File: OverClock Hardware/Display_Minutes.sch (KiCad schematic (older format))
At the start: 37 parts

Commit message: Completed Schematic and ran ERC
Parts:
- added C28, C29, C30: 10nF, Capacitor_SMD:C_0805_2012Metric_Pad1.15x1.40mm_HandSolder, symbol Device:C_Small
- gave numbers to parts that had none: 37
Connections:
- net GND: now also C28.2, C29.2, C30.2
- net +3V: now reaches U3.43 (Vcc_IO_3)
- net +3V: now also U3.56 (Vcc_IO_3), U3.64 (Vcc_IO_3), C28.1, C29.1, C30.1

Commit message: Matched symbols to footprints and generated netlist
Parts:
- D3, D4: footprint (none) -> Maxted Libs:DSM7TA56106T
- R27, R28, R29, R30, R31, R32, R33, R34, R35, R36, R37, R38, R39, R40, R41, R42: footprint (none) -> Resistor_SMD:R_0805_2012Metric_Pad1.15x1.40mm_HandSolder
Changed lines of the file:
@@
 F 0 "D3" H 13750 3700 50  0000 R CNN
 F 1 "DSM7TA56106T" H 14350 2250 50  0000 R CNN
-F 2 "" H 14450 2900 50  0001 C CNN
+F 2 "Maxted Libs:DSM7TA56106T" H 14450 2900 50  0001 C CNN
 F 3 "" H 14450 2900 50  0001 C CNN
 	1    14150 2900
@@
 F 0 "R27" H 10459 4496 50  0000 L CNN
 F 1 "1K" H 10459 4405 50  0000 L CNN
-F 2 "" H 10400 4450 50  0001 C CNN
+F 2 "Resistor_SMD:R_0805_2012Metric_Pad1.15x1.40mm_HandSolder" H 10400 4450 50  0001 C CNN
 F 3 "~" H 10400 4450 50  0001 C CNN
 	1    10400 4450
@@
 F 0 "R28" H 11009 4496 50  0000 L CNN
 F 1 "1K" H 11009 4405 50  0000 L CNN
-F 2 "" H 10950 4450 50  0001 C CNN
+F 2 "Resistor_SMD:R_0805_2012Metric_Pad1.15x1.40mm_HandSolder" H 10950 4450 50  0001 C CNN
 F 3 "~" H 10950 4450 50  0001 C CNN
 	1    10950 4450
@@
 F 0 "R29" H 11559 4496 50  0000 L CNN
 F 1 "1K" H 11559 4405 50  0000 L CNN
-F 2 "" H 11500 4450 50  0001 C CNN
+F 2 "Resistor_SMD:R_0805_2012Metric_Pad1.15x1.40mm_HandSolder" H 11500 4450 50  0001 C CNN
 F 3 "~" H 11500 4450 50  0001 C CNN
 	1    11500 4450
@@
 F 0 "R30" H 12109 4496 50  0000 L CNN
 F 1 "1K" H 12109 4405 50  0000 L CNN
-F 2 "" H 12050 4450 50  0001 C CNN
+F 2 "Resistor_SMD:R_0805_2012Metric_Pad1.15x1.40mm_HandSolder" H 12050 4450 50  0001 C CNN
 F 3 "~" H 12050 4450 50  0001 C CNN
 	1    12050 4450
@@
 F 0 "R31" H 12659 4496 50  0000 L CNN
 F 1 "1K" H 12659 4405 50  0000 L CNN
-F 2 "" H 12600 4450 50  0001 C CNN
+F 2 "Resistor_SMD:R_0805_2012Metric_Pad1.15x1.40mm_HandSolder" H 12600 4450 50  0001 C CNN
 F 3 "~" H 12600 4450 50  0001 C CNN
 	1    12600 4450
@@
 F 0 "R32" H 13209 4496 50  0000 L CNN
 F 1 "1K" H 13209 4405 50  0000 L CNN
-F 2 "" H 13150 4450 50  0001 C CNN
+F 2 "Resistor_SMD:R_0805_2012Metric_Pad1.15x1.40mm_HandSolder" H 13150 4450 50  0001 C CNN
 F 3 "~" H 13150 4450 50  0001 C CNN
 	1    13150 4450
@@
 F 0 "R33" H 13759 4496 50  0000 L CNN
 F 1 "1K" H 13759 4405 50  0000 L CNN
-F 2 "" H 13700 4450 50  0001 C CNN
+F 2 "Resistor_SMD:R_0805_2012Metric_Pad1.15x1.40mm_HandSolder" H 13700 4450 50  0001 C CNN
 F 3 "~" H 13700 4450 50  0001 C CNN
 	1    13700 4450
@@
 F 0 "R34" H 14359 4496 50  0000 L CNN
 F 1 "1K" H 14359 4405 50  0000 L CNN
-F 2 "" H 14300 4450 50  0001 C CNN
+F 2 "Resistor_SMD:R_0805_2012Metric_Pad1.15x1.40mm_HandSolder" H 14300 4450 50  0001 C CNN
 F 3 "~" H 14300 4450 50  0001 C CNN
 	1    14300 4450
@@
 F 0 "D4" H 7050 3750 50  0000 R CNN
 F 1 "DSM7TA56106T" H 7650 2300 50  0000 R CNN
-F 2 "" H 7750 2950 50  0001 C CNN
+F 2 "Maxted Libs:DSM7TA56106T" H 7750 2950 50  0001 C CNN
 F 3 "" H 7750 2950 50  0001 C CNN
 	1    7450 2950
@@
 F 0 "R35" H 3759 4546 50  0000 L CNN
 F 1 "1K" H 3759 4455 50  0000 L CNN
-F 2 "" H 3700 4500 50  0001 C CNN
+F 2 "Resistor_SMD:R_0805_2012Metric_Pad1.15x1.40mm_HandSolder" H 3700 4500 50  0001 C CNN
 F 3 "~" H 3700 4500 50  0001 C CNN
 	1    3700 4500
@@
 F 0 "R36" H 4309 4546 50  0000 L CNN
 F 1 "1K" H 4309 4455 50  0000 L CNN
-F 2 "" H 4250 4500 50  0001 C CNN
+F 2 "Resistor_SMD:R_0805_2012Metric_Pad1.15x1.40mm_HandSolder" H 4250 4500 50  0001 C CNN
 F 3 "~" H 4250 4500 50  0001 C CNN
 	1    4250 4500
@@
 F 0 "R37" H 4859 4546 50  0000 L CNN
 F 1 "1K" H 4859 4455 50  0000 L CNN
-F 2 "" H 4800 4500 50  0001 C CNN
+F 2 "Resistor_SMD:R_0805_2012Metric_Pad1.15x1.40mm_HandSolder" H 4800 4500 50  0001 C CNN
 F 3 "~" H 4800 4500 50  0001 C CNN
 	1    4800 4500
@@
 F 0 "R38" H 5409 4546 50  0000 L CNN
 F 1 "1K" H 5409 4455 50  0000 L CNN
-F 2 "" H 5350 4500 50  0001 C CNN
+F 2 "Resistor_SMD:R_0805_2012Metric_Pad1.15x1.40mm_HandSolder" H 5350 4500 50  0001 C CNN
 F 3 "~" H 5350 4500 50  0001 C CNN
 	1    5350 4500
@@
 F 0 "R39" H 5959 4546 50  0000 L CNN
 F 1 "1K" H 5959 4455 50  0000 L CNN
-F 2 "" H 5900 4500 50  0001 C CNN
+F 2 "Resistor_SMD:R_0805_2012Metric_Pad1.15x1.40mm_HandSolder" H 5900 4500 50  0001 C CNN
 F 3 "~" H 5900 4500 50  0001 C CNN
 	1    5900 4500
@@
 F 0 "R40" H 6509 4546 50  0000 L CNN
 F 1 "1K" H 6509 4455 50  0000 L CNN
-F 2 "" H 6450 4500 50  0001 C CNN
+F 2 "Resistor_SMD:R_0805_2012Metric_Pad1.15x1.40mm_HandSolder" H 6450 4500 50  0001 C CNN
 F 3 "~" H 6450 4500 50  0001 C CNN
 	1    6450 4500
@@
 F 0 "R41" H 7059 4546 50  0000 L CNN
 F 1 "1K" H 7059 4455 50  0000 L CNN
-F 2 "" H 7000 4500 50  0001 C CNN
+F 2 "Resistor_SMD:R_0805_2012Metric_Pad1.15x1.40mm_HandSolder" H 7000 4500 50  0001 C CNN
 F 3 "~" H 7000 4500 50  0001 C CNN
 	1    7000 4500
@@
 F 0 "R42" H 7659 4546 50  0000 L CNN
 F 1 "1K" H 7659 4455 50  0000 L CNN
-F 2 "" H 7600 4500 50  0001 C CNN
+F 2 "Resistor_SMD:R_0805_2012Metric_Pad1.15x1.40mm_HandSolder" H 7600 4500 50  0001 C CNN
 F 3 "~" H 7600 4500 50  0001 C CNN
 	1    7600 4500

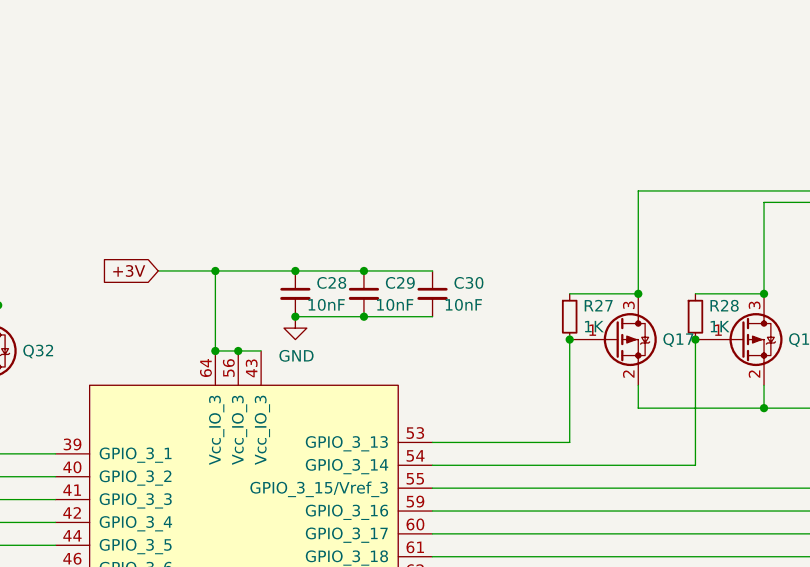
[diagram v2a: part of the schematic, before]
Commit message: Place and route Decoupling Capacitors
Placed and routed all the decoupling capacitors for the FPGA. Created Top and bottom GND planes too for better signal integrity
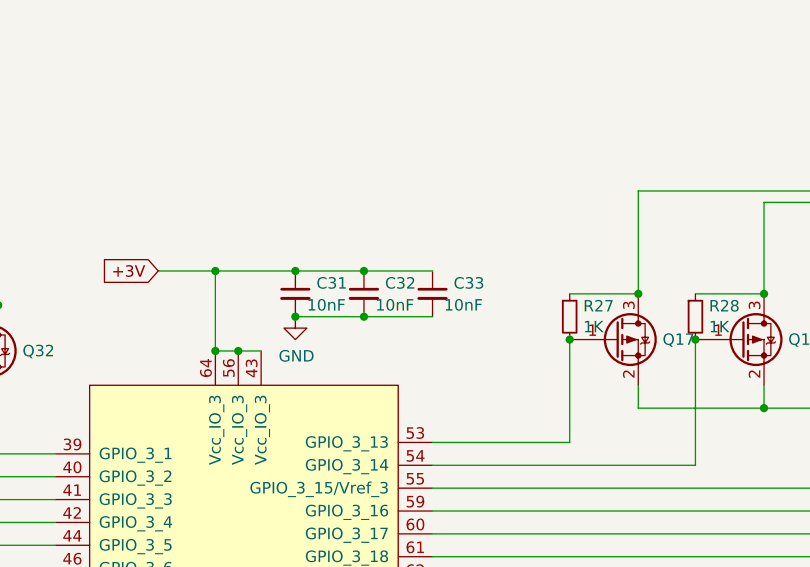
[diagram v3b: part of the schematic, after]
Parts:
- C31: renamed from C28; footprint Capacitor_SMD:C_0805_2012Metric_Pad1.15x1.40mm_HandSolder -> Capacitor_SMD:C_0603_1608Metric_Pad1.05x0.95mm_HandSolder
- C32: renamed from C29; footprint Capacitor_SMD:C_0805_2012Metric_Pad1.15x1.40mm_HandSolder -> Capacitor_SMD:C_0603_1608Metric_Pad1.05x0.95mm_HandSolder
- C33: renamed from C30; footprint Capacitor_SMD:C_0805_2012Metric_Pad1.15x1.40mm_HandSolder -> Capacitor_SMD:C_0603_1608Metric_Pad1.05x0.95mm_HandSolder
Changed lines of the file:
@@
 AR Path="/5C66B7E8/5C9F0D8B" Ref="#PWR?"  Part="1"
 AR Path="/5C87E0ED/5C9F0D8B" Ref="#PWR?"  Part="1"
-AR Path="/5C9EFB73/5C9F0D8B" Ref="#PWR018"  Part="1"
-F 0 "#PWR018" H 14250 1750 50  0001 C CNN
+AR Path="/5C9EFB73/5C9F0D8B" Ref="#PWR019"  Part="1"
+F 0 "#PWR019" H 14250 1750 50  0001 C CNN
 F 1 "+4V" H 14265 2073 50  0000 C CNN
 F 2 "" H 14250 1900 50  0001 C CNN
@@
 AR Path="/5C66B7E8/5C9F0DB7" Ref="#PWR?"  Part="1"
 AR Path="/5C87E0ED/5C9F0DB7" Ref="#PWR?"  Part="1"
-AR Path="/5C9EFB73/5C9F0DB7" Ref="#PWR021"  Part="1"
-F 0 "#PWR021" H 12500 4600 50  0001 C CNN
+AR Path="/5C9EFB73/5C9F0DB7" Ref="#PWR022"  Part="1"
+F 0 "#PWR022" H 12500 4600 50  0001 C CNN
 F 1 "GND" H 12505 4677 50  0000 C CNN
 F 2 "" H 12500 4850 50  0001 C CNN
@@
 AR Path="/5C66B7E8/5C9F3321" Ref="#PWR?"  Part="1"
 AR Path="/5C87E0ED/5C9F3321" Ref="#PWR?"  Part="1"
-AR Path="/5C9EFB73/5C9F3321" Ref="#PWR019"  Part="1"
-F 0 "#PWR019" H 7550 1800 50  0001 C CNN
+AR Path="/5C9EFB73/5C9F3321" Ref="#PWR020"  Part="1"
+F 0 "#PWR020" H 7550 1800 50  0001 C CNN
 F 1 "+4V" H 7565 2123 50  0000 C CNN
 F 2 "" H 7550 1950 50  0001 C CNN
@@
 AR Path="/5C66B7E8/5C9F334D" Ref="#PWR?"  Part="1"
 AR Path="/5C87E0ED/5C9F334D" Ref="#PWR?"  Part="1"
-AR Path="/5C9EFB73/5C9F334D" Ref="#PWR022"  Part="1"
-F 0 "#PWR022" H 5800 4650 50  0001 C CNN
+AR Path="/5C9EFB73/5C9F334D" Ref="#PWR023"  Part="1"
+F 0 "#PWR023" H 5800 4650 50  0001 C CNN
 F 1 "GND" H 5805 4727 50  0000 C CNN
 F 2 "" H 5800 4900 50  0001 C CNN
@@
 	8950 4600 8850 4600
 $Comp
-L Device:C_Small C29
+L Device:C_Small C32
 U 1 1 5CB8F75B
 P 9500 4350
-F 0 "C29" H 9592 4396 50  0000 L CNN
+F 0 "C32" H 9592 4396 50  0000 L CNN
 F 1 "10nF" H 9550 4300 50  0000 L CNN
-F 2 "Capacitor_SMD:C_0805_2012Metric_Pad1.15x1.40mm_HandSolder" H 9500 4350 50  0001 C CNN
+F 2 "Capacitor_SMD:C_0603_1608Metric_Pad1.05x0.95mm_HandSolder" H 9500 4350 50  0001 C CNN
 F 3 "~" H 9500 4350 50  0001 C CNN
 	1    9500 4350
@@
 $EndComp
 $Comp
-L Device:C_Small C30
+L Device:C_Small C33
 U 1 1 5CB8F8E1
 P 9800 4350
-F 0 "C30" H 9892 4396 50  0000 L CNN
+F 0 "C33" H 9892 4396 50  0000 L CNN
 F 1 "10nF" H 9850 4300 50  0000 L CNN
-F 2 "Capacitor_SMD:C_0805_2012Metric_Pad1.15x1.40mm_HandSolder" H 9800 4350 50  0001 C CNN
+F 2 "Capacitor_SMD:C_0603_1608Metric_Pad1.05x0.95mm_HandSolder" H 9800 4350 50  0001 C CNN
 F 3 "~" H 9800 4350 50  0001 C CNN
 	1    9800 4350
@@
 $EndComp
 $Comp
-L Device:C_Small C28
+L Device:C_Small C31
 U 1 1 5CB98270
 P 9200 4350
-F 0 "C28" H 9292 4396 50  0000 L CNN
+F 0 "C31" H 9292 4396 50  0000 L CNN
 F 1 "10nF" H 9250 4300 50  0000 L CNN
-F 2 "Capacitor_SMD:C_0805_2012Metric_Pad1.15x1.40mm_HandSolder" H 9200 4350 50  0001 C CNN
+F 2 "Capacitor_SMD:C_0603_1608Metric_Pad1.05x0.95mm_HandSolder" H 9200 4350 50  0001 C CNN
 F 3 "~" H 9200 4350 50  0001 C CNN
 	1    9200 4350
@@
 	9500 4450 9200 4450
 $Comp
-L power:GND #PWR020
+L power:GND #PWR021
 U 1 1 5CBB2B7C
 P 9200 4450
-F 0 "#PWR020" H 9200 4200 50  0001 C CNN
+F 0 "#PWR021" H 9200 4200 50  0001 C CNN
 F 1 "GND" H 9205 4277 50  0000 C CNN
 F 2 "" H 9200 4450 50  0001 C CNN

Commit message: Completed Initial Routing
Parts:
- R27, R28, R29, R30, R31, R32, R33, R34, R35, R36, R37, R38, R39, R40, R41, R42: footprint Resistor_SMD:R_0805_2012Metric_Pad1.15x1.40mm_HandSolder -> Resistor_SMD:R_0603_1608Metric_Pad1.05x0.95mm_HandSolder
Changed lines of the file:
@@
 F 0 "R27" H 10459 4496 50  0000 L CNN
 F 1 "1K" H 10459 4405 50  0000 L CNN
-F 2 "Resistor_SMD:R_0805_2012Metric_Pad1.15x1.40mm_HandSolder" H 10400 4450 50  0001 C CNN
+F 2 "Resistor_SMD:R_0603_1608Metric_Pad1.05x0.95mm_HandSolder" H 10400 4450 50  0001 C CNN
 F 3 "~" H 10400 4450 50  0001 C CNN
 	1    10400 4450
@@
 F 0 "R28" H 11009 4496 50  0000 L CNN
 F 1 "1K" H 11009 4405 50  0000 L CNN
-F 2 "Resistor_SMD:R_0805_2012Metric_Pad1.15x1.40mm_HandSolder" H 10950 4450 50  0001 C CNN
+F 2 "Resistor_SMD:R_0603_1608Metric_Pad1.05x0.95mm_HandSolder" H 10950 4450 50  0001 C CNN
 F 3 "~" H 10950 4450 50  0001 C CNN
 	1    10950 4450
@@
 F 0 "R29" H 11559 4496 50  0000 L CNN
 F 1 "1K" H 11559 4405 50  0000 L CNN
-F 2 "Resistor_SMD:R_0805_2012Metric_Pad1.15x1.40mm_HandSolder" H 11500 4450 50  0001 C CNN
+F 2 "Resistor_SMD:R_0603_1608Metric_Pad1.05x0.95mm_HandSolder" H 11500 4450 50  0001 C CNN
 F 3 "~" H 11500 4450 50  0001 C CNN
 	1    11500 4450
@@
 F 0 "R30" H 12109 4496 50  0000 L CNN
 F 1 "1K" H 12109 4405 50  0000 L CNN
-F 2 "Resistor_SMD:R_0805_2012Metric_Pad1.15x1.40mm_HandSolder" H 12050 4450 50  0001 C CNN
+F 2 "Resistor_SMD:R_0603_1608Metric_Pad1.05x0.95mm_HandSolder" H 12050 4450 50  0001 C CNN
 F 3 "~" H 12050 4450 50  0001 C CNN
 	1    12050 4450
@@
 F 0 "R31" H 12659 4496 50  0000 L CNN
 F 1 "1K" H 12659 4405 50  0000 L CNN
-F 2 "Resistor_SMD:R_0805_2012Metric_Pad1.15x1.40mm_HandSolder" H 12600 4450 50  0001 C CNN
+F 2 "Resistor_SMD:R_0603_1608Metric_Pad1.05x0.95mm_HandSolder" H 12600 4450 50  0001 C CNN
 F 3 "~" H 12600 4450 50  0001 C CNN
 	1    12600 4450
@@
 F 0 "R32" H 13209 4496 50  0000 L CNN
 F 1 "1K" H 13209 4405 50  0000 L CNN
-F 2 "Resistor_SMD:R_0805_2012Metric_Pad1.15x1.40mm_HandSolder" H 13150 4450 50  0001 C CNN
+F 2 "Resistor_SMD:R_0603_1608Metric_Pad1.05x0.95mm_HandSolder" H 13150 4450 50  0001 C CNN
 F 3 "~" H 13150 4450 50  0001 C CNN
 	1    13150 4450
@@
 F 0 "R33" H 13759 4496 50  0000 L CNN
 F 1 "1K" H 13759 4405 50  0000 L CNN
-F 2 "Resistor_SMD:R_0805_2012Metric_Pad1.15x1.40mm_HandSolder" H 13700 4450 50  0001 C CNN
+F 2 "Resistor_SMD:R_0603_1608Metric_Pad1.05x0.95mm_HandSolder" H 13700 4450 50  0001 C CNN
 F 3 "~" H 13700 4450 50  0001 C CNN
 	1    13700 4450
@@
 F 0 "R34" H 14359 4496 50  0000 L CNN
 F 1 "1K" H 14359 4405 50  0000 L CNN
-F 2 "Resistor_SMD:R_0805_2012Metric_Pad1.15x1.40mm_HandSolder" H 14300 4450 50  0001 C CNN
+F 2 "Resistor_SMD:R_0603_1608Metric_Pad1.05x0.95mm_HandSolder" H 14300 4450 50  0001 C CNN
 F 3 "~" H 14300 4450 50  0001 C CNN
 	1    14300 4450
@@
 F 0 "R35" H 3759 4546 50  0000 L CNN
 F 1 "1K" H 3759 4455 50  0000 L CNN
-F 2 "Resistor_SMD:R_0805_2012Metric_Pad1.15x1.40mm_HandSolder" H 3700 4500 50  0001 C CNN
+F 2 "Resistor_SMD:R_0603_1608Metric_Pad1.05x0.95mm_HandSolder" H 3700 4500 50  0001 C CNN
 F 3 "~" H 3700 4500 50  0001 C CNN
 	1    3700 4500
@@
 F 0 "R36" H 4309 4546 50  0000 L CNN
 F 1 "1K" H 4309 4455 50  0000 L CNN
-F 2 "Resistor_SMD:R_0805_2012Metric_Pad1.15x1.40mm_HandSolder" H 4250 4500 50  0001 C CNN
+F 2 "Resistor_SMD:R_0603_1608Metric_Pad1.05x0.95mm_HandSolder" H 4250 4500 50  0001 C CNN
 F 3 "~" H 4250 4500 50  0001 C CNN
 	1    4250 4500
@@
 F 0 "R37" H 4859 4546 50  0000 L CNN
 F 1 "1K" H 4859 4455 50  0000 L CNN
-F 2 "Resistor_SMD:R_0805_2012Metric_Pad1.15x1.40mm_HandSolder" H 4800 4500 50  0001 C CNN
+F 2 "Resistor_SMD:R_0603_1608Metric_Pad1.05x0.95mm_HandSolder" H 4800 4500 50  0001 C CNN
 F 3 "~" H 4800 4500 50  0001 C CNN
 	1    4800 4500
@@
 F 0 "R38" H 5409 4546 50  0000 L CNN
 F 1 "1K" H 5409 4455 50  0000 L CNN
-F 2 "Resistor_SMD:R_0805_2012Metric_Pad1.15x1.40mm_HandSolder" H 5350 4500 50  0001 C CNN
+F 2 "Resistor_SMD:R_0603_1608Metric_Pad1.05x0.95mm_HandSolder" H 5350 4500 50  0001 C CNN
 F 3 "~" H 5350 4500 50  0001 C CNN
 	1    5350 4500
@@
 F 0 "R39" H 5959 4546 50  0000 L CNN
 F 1 "1K" H 5959 4455 50  0000 L CNN
-F 2 "Resistor_SMD:R_0805_2012Metric_Pad1.15x1.40mm_HandSolder" H 5900 4500 50  0001 C CNN
+F 2 "Resistor_SMD:R_0603_1608Metric_Pad1.05x0.95mm_HandSolder" H 5900 4500 50  0001 C CNN
 F 3 "~" H 5900 4500 50  0001 C CNN
 	1    5900 4500
@@
 F 0 "R40" H 6509 4546 50  0000 L CNN
 F 1 "1K" H 6509 4455 50  0000 L CNN
-F 2 "Resistor_SMD:R_0805_2012Metric_Pad1.15x1.40mm_HandSolder" H 6450 4500 50  0001 C CNN
+F 2 "Resistor_SMD:R_0603_1608Metric_Pad1.05x0.95mm_HandSolder" H 6450 4500 50  0001 C CNN
 F 3 "~" H 6450 4500 50  0001 C CNN
 	1    6450 4500
@@
 F 0 "R41" H 7059 4546 50  0000 L CNN
 F 1 "1K" H 7059 4455 50  0000 L CNN
-F 2 "Resistor_SMD:R_0805_2012Metric_Pad1.15x1.40mm_HandSolder" H 7000 4500 50  0001 C CNN
+F 2 "Resistor_SMD:R_0603_1608Metric_Pad1.05x0.95mm_HandSolder" H 7000 4500 50  0001 C CNN
 F 3 "~" H 7000 4500 50  0001 C CNN
 	1    7000 4500
@@
 F 0 "R42" H 7659 4546 50  0000 L CNN
 F 1 "1K" H 7659 4455 50  0000 L CNN
-F 2 "Resistor_SMD:R_0805_2012Metric_Pad1.15x1.40mm_HandSolder" H 7600 4500 50  0001 C CNN
+F 2 "Resistor_SMD:R_0603_1608Metric_Pad1.05x0.95mm_HandSolder" H 7600 4500 50  0001 C CNN
 F 3 "~" H 7600 4500 50  0001 C CNN
 	1    7600 4500
